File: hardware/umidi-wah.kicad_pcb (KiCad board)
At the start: 2 copper layers, 128 x 101 mm, 92 parts, among them J1 Power, J10 Midi_thru, J11 Midi_t/o, J12 Midi_out, J2 Pots Main, J3 Pots Front, J4 Switch, J5 Input, J6 Output, J7 Conn_02x05_Odd_Even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

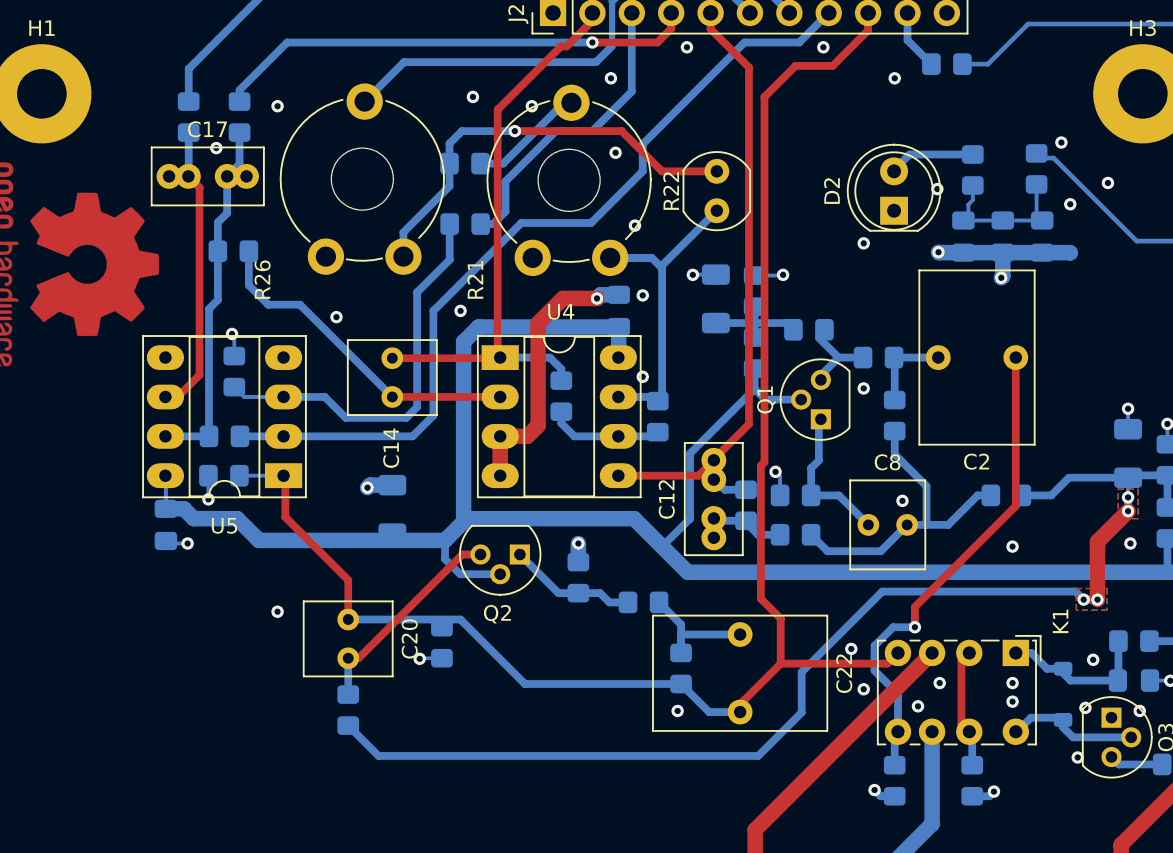
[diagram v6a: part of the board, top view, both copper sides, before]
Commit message: Fix integrator positive input (is now vmid)
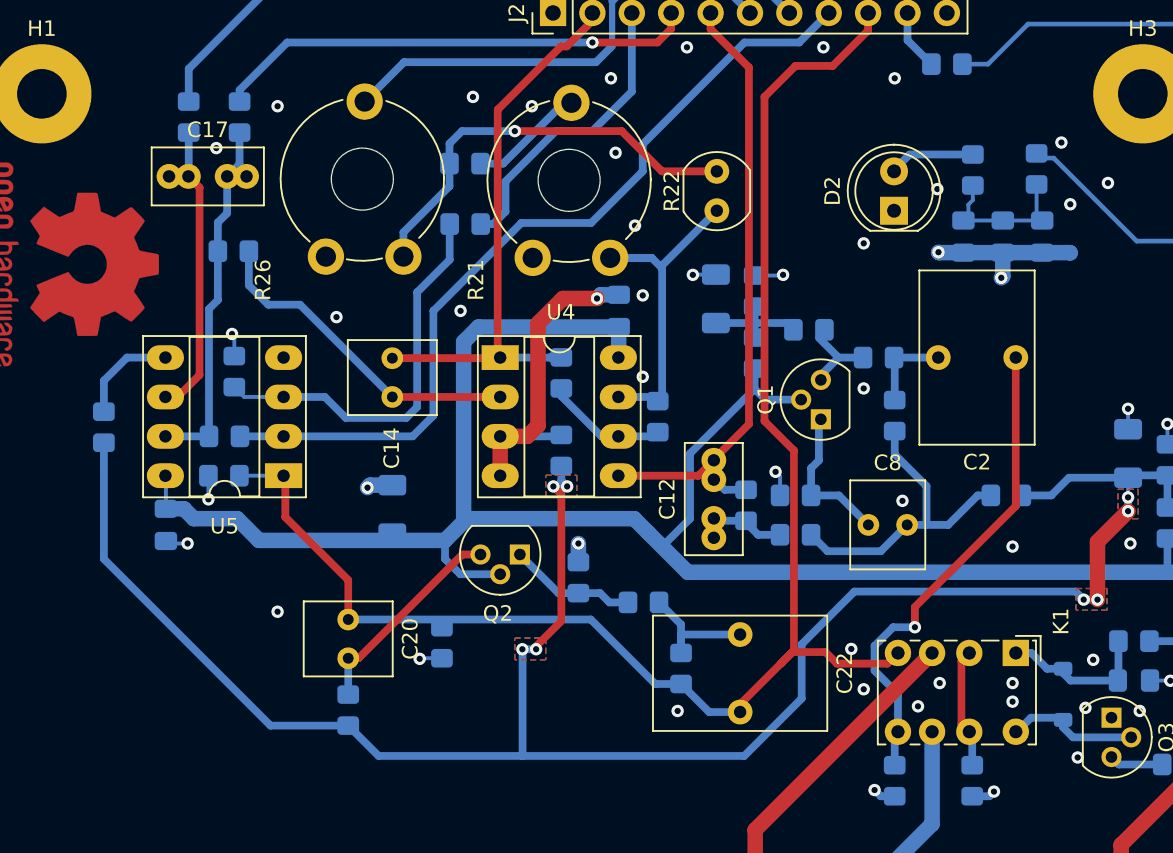
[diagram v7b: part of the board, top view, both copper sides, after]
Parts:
- added R38: 10k, Resistor_SMD:R_0805_2012Metric_Pad1.20x1.40mm_HandSolder, B.Cu at (101.5, 86.0)
- added R39: 10k, Resistor_SMD:R_0805_2012Metric_Pad1.20x1.40mm_HandSolder, B.Cu at (72.0, 84.5)
- moved R13 1.50 mm to (101.5, 81.0)
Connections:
- U4 pad 3: GND -> Net-(U4A-+)
- U5 pad 5: GND -> Net-(U5B-+)
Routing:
- net vmid: track 76.3 -> 126.0 mm, vias 4 -> 8
- net Net-(U5B-+): track 0.00 -> 6.58 mm
- net Net-(U4A-+): track 0.00 -> 3.98 mm
- net /wah_out: track 143.4 -> 144.5 mm
- net /Filter/rv1_1: track 77.7 -> 76.7 mm
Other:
- board text added: "umidi-wah 0.6 {dblquote}demon{dblquote} [2024]"
- board text removed: "umidi-wah 0.5 {dblquote}demon{dblquote} [2024]"

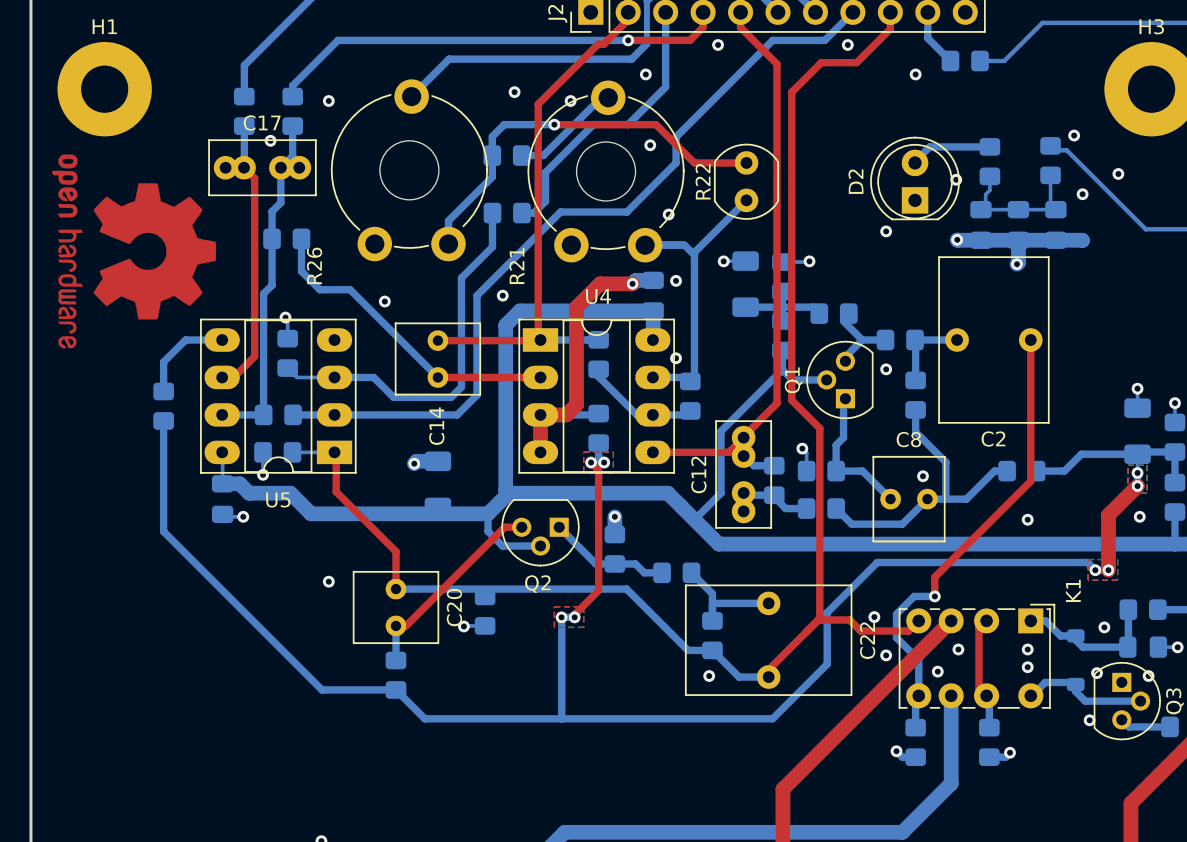
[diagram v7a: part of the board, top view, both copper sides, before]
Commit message: Fix unintended filter_out signal union. Revise some placement.
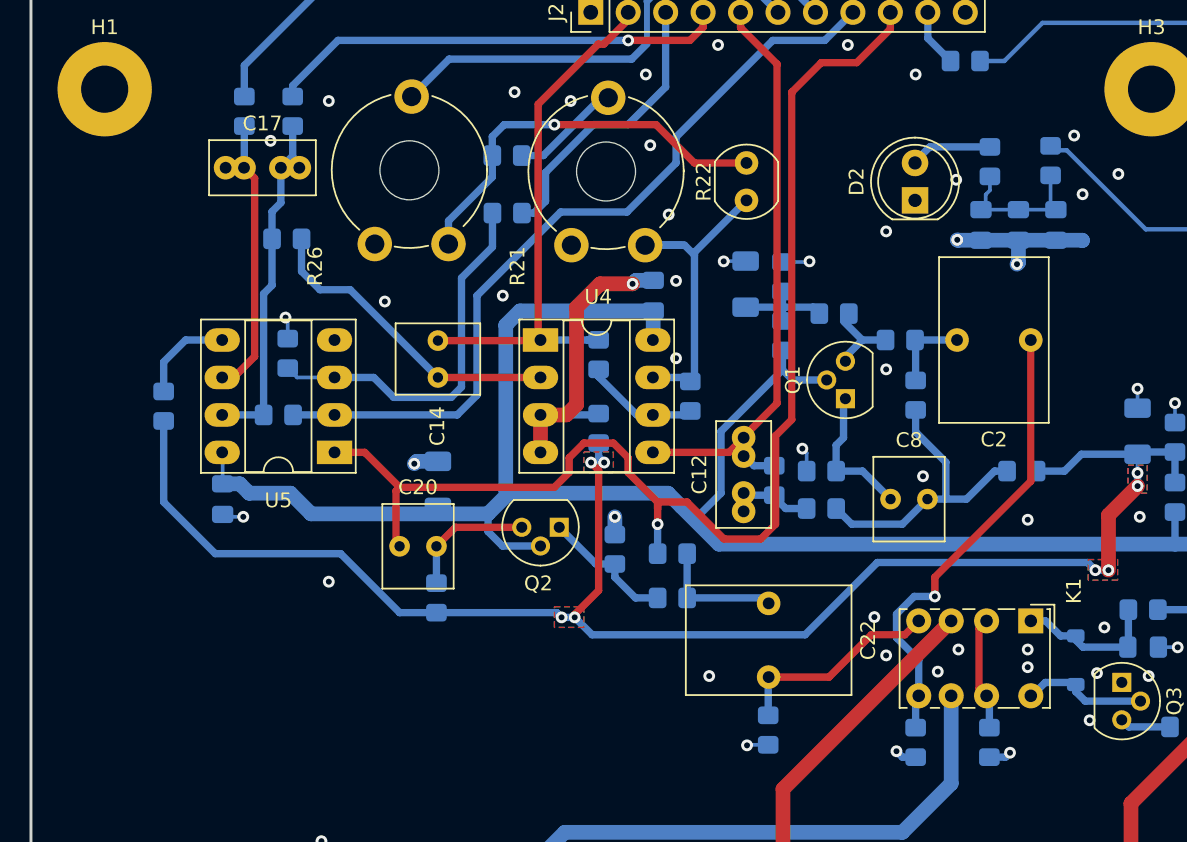
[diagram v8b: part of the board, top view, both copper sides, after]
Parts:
- removed R28: 1M, Resistor_SMD:R_0805_2012Metric_Pad1.20x1.40mm_HandSolder
- removed REF**: OSHW-Logo2_14.6x12mm_Copper, Symbol:OSHW-Logo2_14.6x12mm_Copper
- moved R37 20.8 mm to (113.0, 106.5)
- moved R33 6.19 mm to (106.5, 94.5), turned to 180 degrees
- moved R30 5.92 mm to (90.5, 97.5)
- moved C20 2.91 mm to (88.0, 94.0), turned to 0 degrees
- moved R36 1.73 mm to (106.5, 97.5)
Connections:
- C20 pad 1: /wah_out -> /Filter/rv3_3
- J2 pad 9: /wah_out -> /Filter/rv3_3
- J3 pad 9: /wah_out -> /Filter/rv3_3
- R33 pad 2: /wah_out -> /Filter/rv3_3
- RV3 pad 2: /wah_out -> /Filter/rv3_3
- RV3 pad 3: /wah_out -> /Filter/rv3_3
- U5 pad 1: /wah_out -> /Filter/rv3_3
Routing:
- net /wah_out: track 144.5 -> 14.4 mm
- net /Filter/rv3_3: track 0.00 -> 127.1 mm, vias 0 -> 1
- net vmid: track 126.0 -> 110.3 mm
- net Net-(Q2-B): track 13.6 -> 8.82 mm
- net GND: track 144.7 -> 143.1 mm, vias 125 -> 124
- net Net-(Q2-E): track 8.25 -> 9.18 mm
